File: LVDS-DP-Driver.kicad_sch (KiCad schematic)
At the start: 39 parts

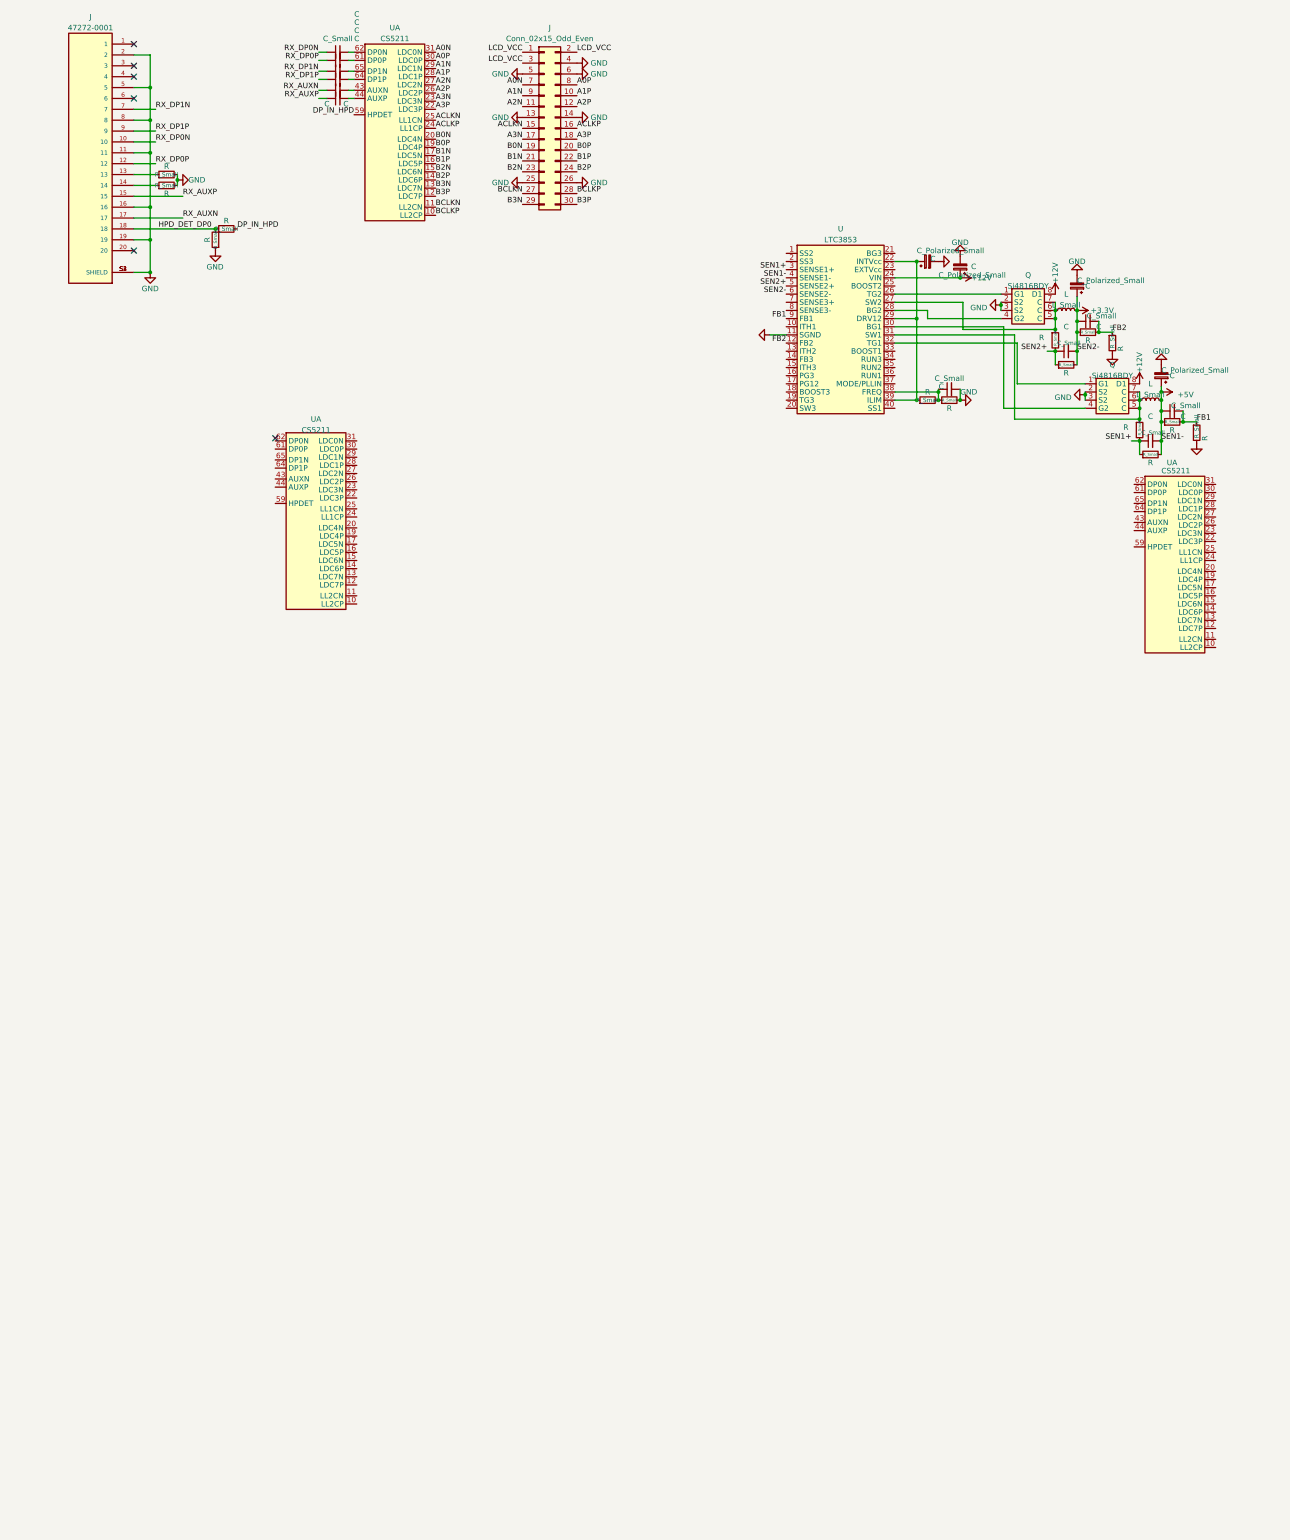
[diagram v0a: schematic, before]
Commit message: MOSFET and Inductors
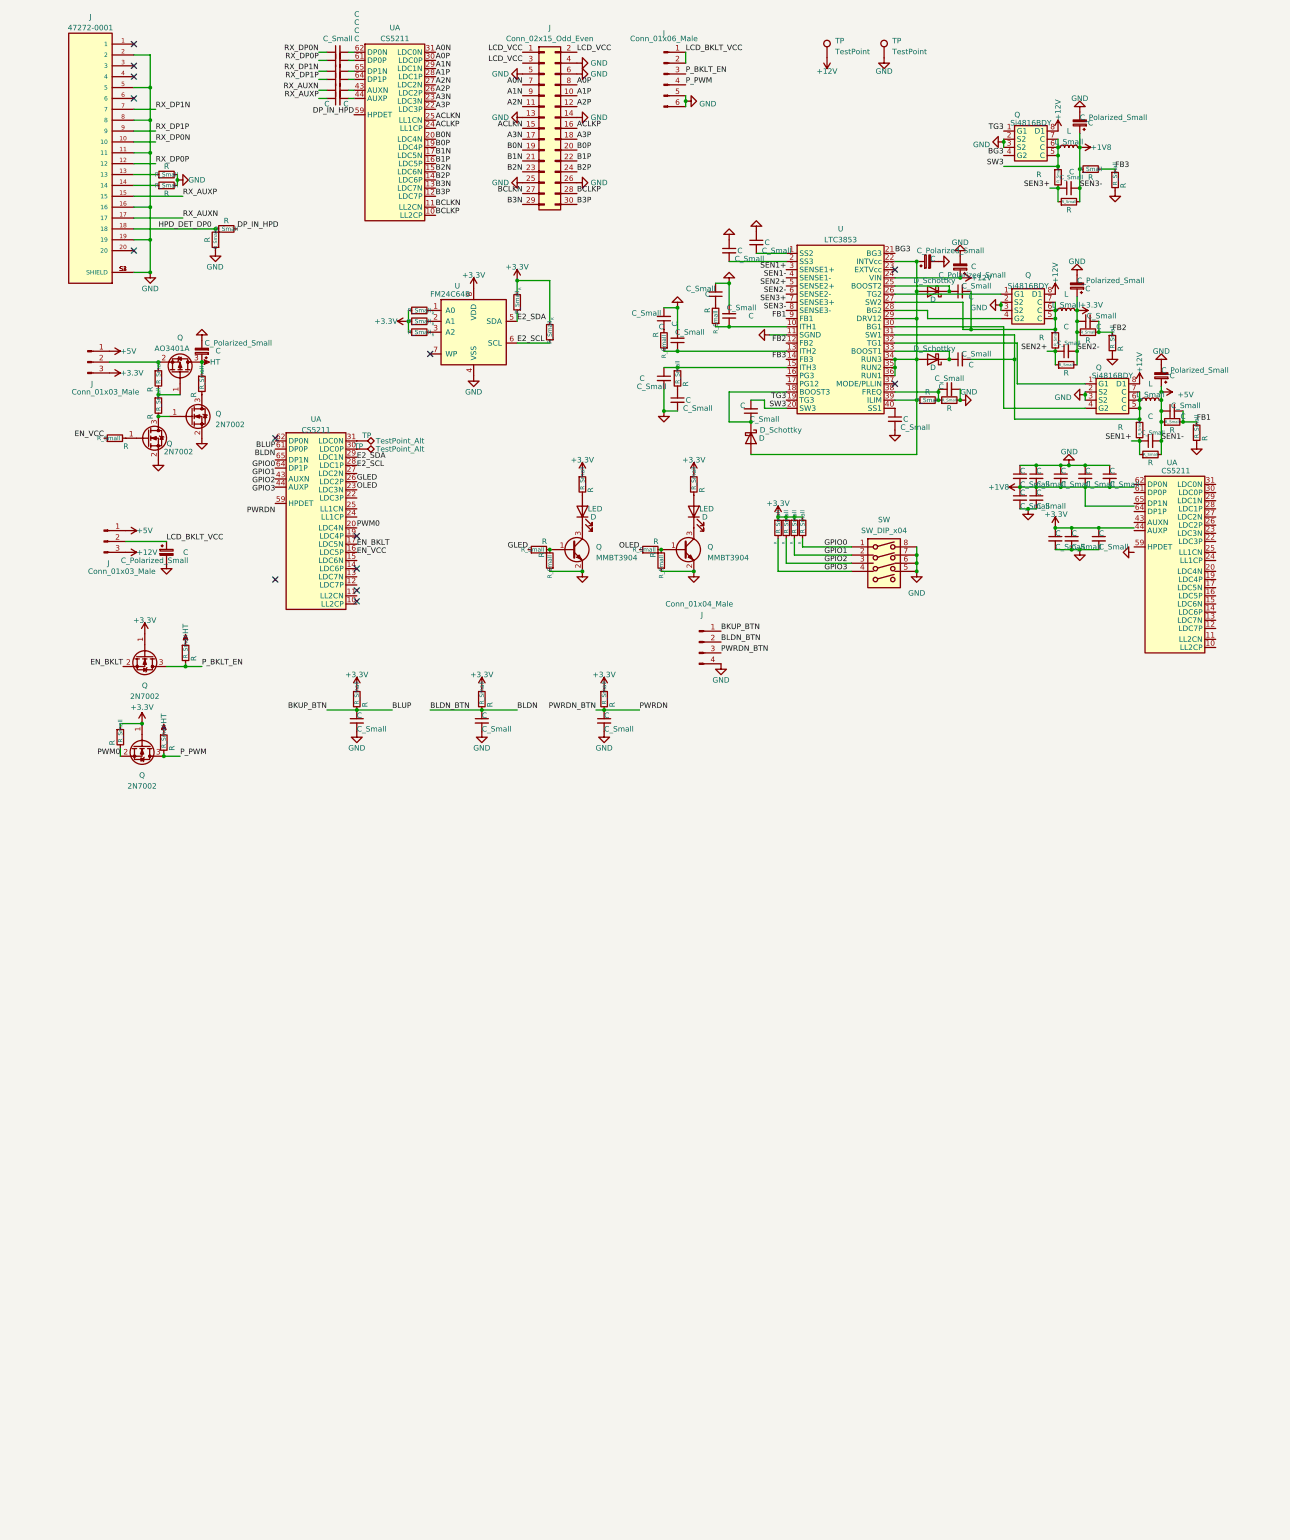
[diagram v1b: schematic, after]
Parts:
- added C (x26): C_Small, symbol Device:C_Small
- added C (x3): C_Polarized_Small, symbol Device:C_Polarized_Small
- added D (x3): D_Schottky, symbol Device:D_Schottky
- added D (x2): LED, symbol Device:LED
- added J (x2): Conn_01x03_Male, symbol Connector:Conn_01x03_Male
- added J: Conn_01x06_Male, symbol Connector:Conn_01x06_Male
- added J: Conn_01x04_Male, symbol Connector:Conn_01x04_Male
- added L: L_Small, symbol Device:L_Small
- added Q: Si4816BDY, symbol Symbols:Si4816BDY
- added Q (x4): 2N7002, Package_TO_SOT_SMD:SOT-23, symbol Transistor_FET:2N7002
- added Q (x2): MMBT3904, Package_TO_SOT_SMD:SOT-23, symbol Transistor_BJT:MMBT3904
- added Q: AO3401A, Package_TO_SOT_SMD:SOT-23, symbol Transistor_FET:AO3401A
- added R (x32): R_Small, symbol Device:R_Small
- added SW: SW_DIP_x04, symbol Switch:SW_DIP_x04
- added TP (x2): TestPoint_Alt, symbol Connector:TestPoint_Alt
- added TP (x2): TestPoint, symbol Connector:TestPoint
- added U: FM24C64B, Package_SO:SOIC-8_3.9x4.9mm_P1.27mm, symbol Memory_NVRAM:FM24C64B
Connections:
- net +12V: now also J.3 (Pin_3), Q.8 (D1), TP.1
- net +3V3: now also C.1, C.1, C.1
- net +5V: now also J.1 (Pin_1), J.1 (Pin_1)
- net GND: now also C.1, C.1, C.1, C.1, C.1, C.1, C.1, C.2, C.2, C.2, C.2, C.2, C.2, C.2, C.2, C.2, C.2, C.2, C.2, C.2, C.2, C.2, C.2, C.2, C.2, J.4 (Pin_4), J.5 (Pin_5), J.6 (Pin_6), Q.2 (E), Q.2 (E), Q.2 (S), Q.2 (S), Q.2 (S2), Q.3 (S2), R.1, R.1, R.2, SW.5, SW.6, SW.7, SW.8, TP.1, U.4 (VSS)
- net at L.1, Q.5 (C), Q.6 (C)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: now also C.2 (x2)
- net at C.1, R.1, U.22 (INTVcc)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: now also U.34 (RUN3), U.35 (RUN2), U.36 (RUN1), D.2 (A), D.2 (A), D.2 (A)
- net PWM0: now reaches U.20 (LDC4N)
- net PWM0: now also Q.2 (S), R.2
- net OLED: now reaches U.23 (LDC3N)
- net OLED: now also R.1
- net GLED: now reaches U.26 (LDC2P)
- net GLED: now also R.1
- net at U.30 (LDC0P): now also TP.1
- net at U.31 (LDC0N): now also TP.1
- net BKUP_BTN: now reaches U.61 (DP0P)
- net BKUP_BTN: now also C.1, J.1 (Pin_1), R.2
- net GPIO0: now reaches U.64 (DP1P)
- net GPIO0: now also R.2, SW.1
- net at U.1 (SS2): now also C.2
- net at U.10 (ITH1): now also C.1, R.1
- net at U.13 (ITH2): now also C.1, R.1
- net FB3: now reaches U.14 (FB3)
- net FB3: now also R.1, R.2
- net at U.15 (ITH3): now also C.1, R.1
- net at U.18 (BOOST3): now also C.1, D.1 (K)
- net TG3: now reaches U.19 (TG3)
- net TG3: now also Q.1 (G1)
- net at U.2 (SS3): now also C.2
- net SW3: now reaches U.20 (SW3)
- net SW3: now also C.2, L.1, Q.5 (C), Q.6 (C), Q.7 (C), R.1
- net BG3: now reaches U.21 (BG3)
- net BG3: now also Q.4 (G2)
- net at U.25 (BOOST2): now also C.1, D.1 (K)
- net at U.33 (BOOST1): now also C.1, D.1 (K)
- net at U.40 (SS1): now also C.1
- net SEN3+: now reaches U.7 (SENSE3+)
- net SEN3+: now also C.1, R.1, R.2
- net +1V8: now reaches U.8 (SENSE3-)
- net +1V8: now also C.1, C.1, C.1, C.2, C.2, C.2, C.2, C.2, C.2, L.2, R.1, R.2
- new net: J.2 (Pin_2), Q.2 (S), R.1
- new net: R.2, U.3 (A2)
- new net: R.2, U.1 (A0)
- new net: Q.1 (G), Q.3 (D), R.2
- new net: Q.3 (D), R.2
- new net: D.1 (K), Q.3 (C) (x2)
- new net: D.2 (A), R.2 (x2)
- new net: Q.1 (B), R.2, R.2 (x2)
- new net: R.2, U.2 (A1)
- new net: C.1, R.2 (x3)
- new net: Q.1 (G), R.1, R.2
- new net: Q.1 (G), R.2
- new net +3.3V: J.3 (Pin_3), Q.1 (G), Q.1 (G), R.1, R.1, R.1, R.1, R.1, R.1, R.1, R.1, R.1, R.1, R.1, R.1, R.1, R.2, R.2, U.8 (VDD)
- new net BLDN: C.1, J.2 (Pin_2), R.2
- new net E2_SCL: R.1, U.6 (SCL)
- new net E2_SDA: R.1, U.5 (SDA)
- new net EN_BKLT: Q.2 (S)
- new net EN_VCC: R.1
- new net GPIO1: R.2, SW.2
- new net GPIO2: R.2, SW.3
- new net GPIO3: R.2, SW.4
- new net HT: C.1, Q.3 (D), R.1, R.1, R.1
- new net LCD_BKLT_VCC: C.1, J.1 (Pin_1), J.2 (Pin_2), J.2 (Pin_2)
- new net PWRDN: C.1, J.3 (Pin_3), R.2
- new net P_BKLT_EN: J.3 (Pin_3), Q.3 (D), R.2
- new net P_PWM: J.4 (Pin_4), Q.3 (D), R.2
- no-connect marks 6 -> 14

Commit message: Changed License to SHL
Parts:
- C1, C10, C13, C2, C22, C23, C24, C27, C28, C29, C3, C31, C32, C33, C34, C36, C38, C39, C4, C42, C43, C44, C5, C6: renamed from C; value C_Small -> 100nF; footprint (none) -> Capacitor_SMD:C_0603_1608Metric
- C11, C15: renamed from C; value C_Small -> 10pF; footprint (none) -> Capacitor_SMD:C_0603_1608Metric
- C12, C14, C26: renamed from C; value C_Polarized_Small -> 330uF; footprint (none) -> Capacitor_Tantalum_SMD:CP_EIA-7343-31_Kemet-D
- C16, C18: renamed from C; value C_Small -> 220pF; footprint (none) -> Capacitor_SMD:C_0603_1608Metric
- C17, C19, C21: renamed from C; value C_Small -> 1.5nF; footprint (none) -> Capacitor_SMD:C_0603_1608Metric
- C20: renamed from C; value C_Small -> 330pF; footprint (none) -> Capacitor_SMD:C_0603_1608Metric
- C25: renamed from C; value C_Small -> 68nF; footprint (none) -> Capacitor_SMD:C_0603_1608Metric
- C30, C35, C37: renamed from C; value C_Small -> 1uF; footprint (none) -> Capacitor_SMD:C_0603_1608Metric
- C40, C45: renamed from C; value C_Polarized_Small -> 10uF; footprint (none) -> Capacitor_Tantalum_SMD:CP_EIA-3528-21_Kemet-B
- C7: renamed from C; value C_Polarized_Small -> 22uF; footprint (none) -> Capacitor_Tantalum_SMD:CP_EIA-3528-21_Kemet-B
- C8: renamed from C; value C_Polarized_Small -> 4.7uF; footprint (none) -> Capacitor_Tantalum_SMD:CP_EIA-3528-21_Kemet-B
- C9: renamed from C; value C_Small -> 1nF; footprint (none) -> Capacitor_SMD:C_0603_1608Metric
- D1, D2, D3: renamed from D; footprint (none) -> Diode_SMD:D_SOD-523
- D4: renamed from D; value LED -> G; footprint (none) -> Diode_SMD:D_0603_1608Metric
- D5: renamed from D; value LED -> O; footprint (none) -> Diode_SMD:D_0603_1608Metric
- J1: renamed from J; footprint MOLEX_47272-0001 -> Footprints:MOLEX_47272-0001
- J2: renamed from J; footprint (none) -> Connector_PinHeader_2.00mm:PinHeader_2x15_P2.00mm_Vertical
- J3: renamed from J; footprint (none) -> Connector_PinHeader_2.54mm:PinHeader_1x06_P2.54mm_Vertical
- J4, J6: renamed from J; footprint (none) -> Connector_PinHeader_2.54mm:PinHeader_1x03_P2.54mm_Vertical
- J5: renamed from J; footprint (none) -> Connector_PinHeader_2.54mm:PinHeader_1x04_P2.54mm_Vertical
- L1, L2: renamed from L; value L_Small -> 3.3uH; footprint (none) -> Inductor_SMD:L_7.3x7.3_H4.5
- L3: renamed from L; value L_Small -> 1.5uH; footprint (none) -> Inductor_SMD:L_1210_3225Metric
- Q1, Q2, Q3: renamed from Q; footprint (none) -> Package_SO:SO-8_3.9x4.9mm_P1.27mm
- R1, R2: renamed from R; value R_Small -> 1M; footprint (none) -> Resistor_SMD:R_0603_1608Metric
- R10, R14, R21: renamed from R; value R_Small -> 20K; footprint (none) -> Resistor_SMD:R_0603_1608Metric
- R11, R7: renamed from R; value R_Small -> 4.75K; footprint (none) -> Resistor_SMD:R_0603_1608Metric
- R12, R8: renamed from R; value R_Small -> 1430; footprint (none) -> Resistor_SMD:R_1206_3216Metric
- R13: renamed from R; value R_Small -> 105K; footprint (none) -> Resistor_SMD:R_0603_1608Metric
- R15: renamed from R; value R_Small -> 15K; footprint (none) -> Resistor_SMD:R_0603_1608Metric
- R16: renamed from R; value R_Small -> 18K; footprint (none) -> Resistor_SMD:R_0603_1608Metric
- R17, R24, R26, R28, R29, R30, R31, R33, R34, R35, R39, R40, R41, R5: renamed from R; value R_Small -> 10K; footprint (none) -> Resistor_SMD:R_0603_1608Metric
- R18: renamed from R; value R_Small -> 2.43K; footprint (none) -> Resistor_SMD:R_0603_1608Metric
- R19: renamed from R; value R_Small -> 1.82K; footprint (none) -> Resistor_SMD:R_0603_1608Metric
- R20: renamed from R; value R_Small -> 25K; footprint (none) -> Resistor_SMD:R_0603_1608Metric
- R22, R23, R25, R27, R3, R36: renamed from R; value R_Small -> 1K; footprint (none) -> Resistor_SMD:R_0603_1608Metric
- R32, R37, R38, R42, R43, R44, R45, R46: renamed from R; value R_Small -> 4K7; footprint (none) -> Resistor_SMD:R_0603_1608Metric
- R4: renamed from R; value R_Small -> 100K; footprint (none) -> Resistor_SMD:R_0603_1608Metric
- R6: renamed from R; value R_Small -> 3.16K; footprint (none) -> Resistor_SMD:R_0603_1608Metric
- R9: renamed from R; value R_Small -> 63.4K; footprint (none) -> Resistor_SMD:R_0603_1608Metric
- SW1: renamed from SW; footprint (none) -> Button_Switch_THT:SW_DIP_SPSTx04_Slide_6.7x11.72mm_W7.62mm_P2.54mm_LowProfile
- TP1: renamed from TP; value TestPoint_Alt -> SMBUS_SDA; footprint (none) -> TestPoint:TestPoint_Pad_1.0x1.0mm
- TP2: renamed from TP; value TestPoint_Alt -> SMBUS_SCL; footprint (none) -> TestPoint:TestPoint_Pad_1.0x1.0mm
- TP3, TP4: renamed from TP; footprint (none) -> TestPoint:TestPoint_Pad_D4.0mm
- U1: renamed from U; footprint (none) -> Package_DFN_QFN:QFN-68-1EP_8x8mm_P0.4mm_EP5.2x5.2mm
- U2: renamed from U; footprint (none) -> Package_DFN_QFN:QFN-40-1EP_6x6mm_P0.5mm_EP4.6x4.6mm
- U3: renamed from U; value FM24C64B -> AT24C64
- renumbered Q to Q10, Q to Q4, Q to Q5, Q to Q6, Q to Q7, Q to Q8, Q to Q9
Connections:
- net +1V8: now also U1.3 (AVDD), U1.4 (AVDD), U1.42 (DVDD), U1.60 (AVDD), U1.66 (AVDD), U1.67 (AVDD), U1.7 (DVDD)
- net +3V3: now also U1.18 (LVDD), U1.32 (LVDD), U1.52 (LVDD)
- net BKUP_BTN: now also U1.56 (BLUP); no longer U1.61 (DP0P)
- net BLDN: now also U1.55 (BLDN)
- net E2_SCL: now also U1.51 (MSCL)
- net E2_SDA: now also U1.50 (MSDA)
- net EN_BKLT: now also U1.46 (EN_BKLT)
- net EN_VCC: now also U1.47 (EN_VCC)
- net GLED: now also U1.57 (GLED); no longer U1.26 (LDC2P)
- net GND: now also U1.21 (GND), U1.35 (GND), U1.40 (GND), U1.45 (GND), U1.63 (GND), U1.69 (GND), U1.8 (GND)
- net GPIO0: now also U1.33 (GPIO0); no longer U1.64 (DP1P)
- net GPIO1: now also U1.34 (GPIO1)
- net GPIO2: now also U1.37 (GPIO2)
- net GPIO3: now also U1.38 (GPIO3)
- net OLED: now also U1.58 (OLED); no longer U1.23 (LDC3N)
- net PWM0: now also U1.48 (PWMOUT0); no longer U1.20 (LDC4N)
- net PWRDN: now also U1.41 (PWRDN)
- net at TP1.1: now also U1.53 (SSDA); no longer U1.31 (LDC0N)
- net at TP2.1: now also U1.54 (SSCL); no longer U1.30 (LDC0P)
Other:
- added sheet DP-Alternate-USB (DP-Alternate-USB.kicad_sch)
